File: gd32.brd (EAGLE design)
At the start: 55 x 70 mm, 23 parts, among them IC1 GD32F450IKH6, IC2 AMS1117-1.5, J1 LCD, U1 W9825G6KH-5

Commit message: Incremental changes
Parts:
- removed POWER1: DC-005, sjg-power:DCJ3P-14.2X11.0X9.0MM
- added +5V_IN: DC-005, sjg-power:DCJ3P-14.2X11.0X9.0MM
- added BOOT_SEL: B3F-1005, SparkFun:TACTILE-PTH
- added BOOT_WHICH: JS202011SCQN, samacsys:JS202011SCQN
- added C10, C9: 10uF/16v, rcl:C0603
- added C11: 0.1uF, rcl:C0201
- added D1: GRN-0402, Seeed-LED:LED-0402
- added JP2: (no value), pinhead:1X02
- added R4: 470R, rcl:R0402
- added R5: 10K, rcl:R0402
- added U$1: GD32_DEBUG, sjg-stm32:SWD_DEBUG
- IC2: value AMS1117-1.5 -> AMS1117-3.3
- moved IC2 40.0 mm to (41.0, 75.5), turned to 0 degrees
- moved POWER 32.4 mm to (26.2, 73.5), turned to 90 degrees
- moved H4 14.1 mm to (61.0, 76.0)
- moved H1 10.0 mm to (4.00, 76.0)
- moved H3 10.0 mm to (61.0, 4.00)
- moved J1 4.00 mm to (28.8, 4.37)
- moved JP1 3.00 mm to (12.0, 4.37)
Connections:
- new net BOOT0: BOOT_SEL.3, BOOT_SEL.4, IC1.D6, R5.2
- new net N$2: D1.+, R4.2
- new net N$3: C10.1, IC2.2, IC2.4, JP2.2, R4.1
- net +3V3: now also BOOT_SEL.1, BOOT_SEL.2, BOOT_WHICH.1, BOOT_WHICH.6, JP2.1, U$1.P1; no longer IC2.2, IC2.4
- net +5V: now also C9.1
- net GND: now also +5V_IN.-1, +5V_IN.-2, BOOT_WHICH.3, BOOT_WHICH.4, C10.2, C11.2, C9.2, R5.1, U$1.P3, U$1.P5, U$1.P9; no longer POWER1.-1, POWER1.-2
- net PA13: now also U$1.P2
- net PA14: now also U$1.P4
- net PB10: now also U$1.P6
- net PB11: now also U$1.P8
- net PB2: now also BOOT_WHICH.2, BOOT_WHICH.5
- net PB4: now also C11.1, U$1.P10
- net V+: now also +5V_IN.+; no longer POWER1.+
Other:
- board size 55 x 70 mm -> 65 x 80 mm
- board text added: "BL"
- board text added: "SRAM"

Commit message: Ready for manufacture
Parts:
- removed C11: 0.1uF, rcl:C0201
- removed JP1: (no value), pinhead:2X02
- removed JP2: (no value), pinhead:1X02
- removed U$1: GD32_DEBUG, sjg-stm32:SWD_DEBUG
- added BL_CTRL, I2C1, SPI0, SPI1, SPI2: (no value), pinhead:2X02
- added C12, C13: 15pF, rcl:C0201
- added C14, C15, C16, C17, C18, C19, C20, C21, C22, C23, C24, C25, C26, C27, C28, C34: 0.1uF, rcl:C0201
- added IO_EXT: (no value), pinhead:2X20
- added PASS_3V3, PASS_RST: (no value), pinhead:1X02
- added PROG: GD32_DEBUG, sjg-stm32:SWD_DEBUG
- added Q2: 8MHz, adafruit:NX3225
- added R37, R8: 1K5, rcl:R0603
- added R6, R7: 10K, rcl:R0402
- added RESET: B3F-1005, SparkFun:TACTILE-PTH
- R2, R3: device rcl:R0805 -> rcl:R0402
- moved R5 10.2 mm to (54.0, 16.6)
- moved R3 7.55 mm to (20.2, 32.1)
- moved R2 7.24 mm to (20.2, 30.9)
- moved IC1 7.09 mm to (29.2, 25.4)
- moved C7 6.50 mm to (38.0, 60.0)
- moved C6 6.46 mm to (38.0, 55.3)
- moved C1 6.14 mm to (20.8, 62.4)
- moved C2 6.11 mm to (20.8, 57.7)
- moved U1 6.08 mm to (29.2, 53.6)
- moved C3 6.08 mm to (20.8, 64.0)
- moved C4 6.08 mm to (20.8, 53.6)
- moved C5 6.08 mm to (20.8, 43.2)
- moved C8 3.24 mm to (3.87, 23.6)
- moved R1 3.24 mm to (5.87, 23.6)
- moved +5V_IN 2.54 mm to (17.0, 69.2)
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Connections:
- net PA11 renamed MCU_USB_N
- net PA12 renamed MCU_USB_P
- removed net PB4: C11.1, IC1.A9, U$1.P10
- removed net PD13: IC1.M15
- removed net PE2: IC1.A2
- removed net PE3: IC1.A1
- removed net PG13: IC1.A8
- removed net PG14: IC1.A7, U1.17
- removed net PG3: IC1.K15
- removed net PG9: IC1.C10
- removed net PH6: IC1.M11
- removed net PH7: IC1.N12
- removed net PI11: IC1.E4
- new net !RST!: IC1.J1, PASS_RST.2, R7.1, RESET.3, RESET.4
- new net N$4: IC1.C6, R6.1
- new net N$5: PASS_RST.1, PROG.P10
- net +3V3: now also BL_CTRL.1, C14.1, C15.1, C16.1, C17.1, C18.1, C19.1, C20.1, C21.1, C22.1, C23.1, C24.1, C25.1, C26.1, C27.1, C28.1, C34.1, I2C1.1, IC1.C1, IC1.C5, IC1.C7, IC1.C8, IC1.C9, IC1.F3, IC1.G13, IC1.G3, IC1.H13, IC1.J12, IC1.J13, IC1.K4, IC1.N10, IC1.N8, IC1.N9, IC1.P1, IC1.R1, IO_EXT.2, PASS_3V3.1, PROG.P1, R37.2, R6.2, R7.2, R8.2; no longer JP1.1, JP2.1, U$1.P1
- net +5V: now also IO_EXT.1
- net GND: now also C12.2, C13.2, C14.2, C15.2, C16.2, C17.2, C18.2, C19.2, C20.2, C21.2, C22.2, C23.2, C24.2, C25.2, C26.2, C27.2, C28.2, C34.2, D1.-, I2C1.3, IC1.D5, IC1.D7, IC1.D8, IC1.D9, IC1.F10, IC1.F12, IC1.F2, IC1.F6, IC1.F7, IC1.F8, IC1.F9, IC1.G10, IC1.G12, IC1.G2, IC1.G6, IC1.G7, IC1.G8, IC1.G9, IC1.H10, IC1.H12, IC1.H6, IC1.H7, IC1.H8, IC1.H9, IC1.J10, IC1.J6, IC1.J7, IC1.J8, IC1.J9, IC1.K10, IC1.K6, IC1.K7, IC1.K8, IC1.K9, IC1.M1, IC1.M8, IC1.M9, IC1.N1, IO_EXT.19, IO_EXT.20, IO_EXT.39, IO_EXT.40, PROG.P3, PROG.P5, PROG.P9, Q2.2, Q2.4, RESET.1, RESET.2, SPI0.3, SPI1.3, SPI2.3; no longer C11.2, U$1.P3, U$1.P5, U$1.P9
- net LCD_BL: now also BL_CTRL.2, BL_CTRL.4; no longer JP1.2, JP1.4
- net N$3: now also PASS_3V3.2; no longer JP2.2
- net PA0: now also IO_EXT.37
- net PA1: now also IO_EXT.38
- net PA13: now also PROG.P2; no longer U$1.P2
- net PA14: now also PROG.P4; no longer U$1.P4
- net PA15: now also IO_EXT.31
- net PA2: now also IO_EXT.35
- net PA3: now also IO_EXT.36
- net PA4: now also BL_CTRL.3; no longer JP1.3
- net PA5: now also SPI0.2
- net PA6: now also SPI0.4
- net PA7: now also SPI0.1
- net PA8: now also IO_EXT.33
- net PA9: now also IO_EXT.34
- net PB0: now also IO_EXT.32
- net PB1: now also IO_EXT.29
- net PB10: now also PROG.P6; no longer U$1.P6
- net PB11: now also PROG.P8; no longer U$1.P8
- net PB12: now also IO_EXT.26
- net PB13: now also SPI1.2
- net PB14: now also SPI1.4
- net PB15: now also SPI1.1
- net PB3: now also IO_EXT.30
- net PB7: now also IO_EXT.27
- net PB8: now also IO_EXT.28
- net PB9: now also IO_EXT.25
- net PC0: now also IO_EXT.23
- net PC1: now also IO_EXT.24
- net PC10: now also SPI2.2
- net PC11: now also SPI2.4
- net PC12: now also SPI2.1
- net PC13: now also IO_EXT.11
- net PC14: now also IO_EXT.12
- net PC15: now also IO_EXT.9
- net PC2: now also IO_EXT.21
- net PC3: now also IO_EXT.22
- net PC4: now also IO_EXT.17
- net PC5: now also IO_EXT.18
- net PC6: now also IO_EXT.15
- net PC7: now also IO_EXT.16
- net PC8: now also IO_EXT.13
- net PC9: now also IO_EXT.14
- net PD11: now also IO_EXT.3
- net PD12: now also IO_EXT.4
- net PD2: now also IO_EXT.10
- net PD3: now also IO_EXT.7
- net PD4: now also IO_EXT.8
- net PD6: now also IO_EXT.5
- net PD7: now also IO_EXT.6
- net PG15: now also U1.17
- net PH0: now also C12.1, Q2.1; no longer J1.40
- net PH1: now also C13.1, Q2.3; no longer J1.39
- net PH4: now also I2C1.2, R8.1
- net PH5: now also I2C1.4, R37.1
- net PI3: now also J1.40
- net PI8: now also J1.39
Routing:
- net PA5: track 0.00 -> 180.4 mm, vias 0 -> 2
- net +5V: track 0.00 -> 161.0 mm
- net PI3: track 0.00 -> 160.3 mm, vias 0 -> 8
- net PB10: track 0.00 -> 148.8 mm, vias 0 -> 4
- net PB11: track 0.00 -> 127.7 mm, vias 0 -> 4
- net PD7: track 0.00 -> 121.6 mm, vias 0 -> 3
- net PA4: track 0.00 -> 117.4 mm, vias 0 -> 6
- net PB8: track 0.00 -> 114.8 mm, vias 0 -> 5
- net PD3: track 0.00 -> 112.4 mm, vias 0 -> 6
- net GND: track 0.00 -> 108.5 mm, vias 0 -> 84
- net PB3: track 0.00 -> 105.1 mm, vias 0 -> 4
- net PD2: track 0.00 -> 103.1 mm, vias 0 -> 5
- net PF1: track 0.00 -> 101.4 mm, vias 0 -> 6
- net PD4: track 0.00 -> 100.1 mm, vias 0 -> 5
- net PC13: track 0.00 -> 98.1 mm, vias 0 -> 5
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- added copper zone on layer 15, net +3V3
- added copper zone on layer 2, net GND
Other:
- board text added: ""Atomic" RGB i/o"
- board text added: "+3V3"
- board text added: "+3v3"
- board text added: "+5V"
- board text added: "1"
- board text added: "40"
- board text added: "CK"
- board text added: "GD32-LCD v 0.1 © 2022 SjG"
- board text added: "GND"
- board text added: "ON"
- board text added: "PA0"
- board text added: "PA1"
- board text added: "PA15"
- board text added: "PA2"
- board text added: "PA3"
- board text added: "PA4"
- board text added: "PA8"
- board text added: "PA9"
- board text added: "PB0"
- board text added: "PB1"
- board text added: "PB12"
- board text added: "PB3"
- board text added: "PB7"
- board text added: "PB8"
- board text added: "PB9"
- board text added: "PC0"
- board text added: "PC1"
- board text added: "PC13"
- board text added: "PC14"
- board text added: "PC15"
- board text added: "PC2"
- board text added: "PC3"
- board text added: "PC4"
- board text added: "PC5"
- board text added: "PC6"
- board text added: "PC7"
- board text added: "PC8"
- board text added: "PC9"
- board text added: "PD11"
- board text added: "PD12"
- board text added: "PD2"
- board text added: "PD3"
- board text added: "PD4"
- board text added: "PD6"
- board text added: "PD7"
- board text added: "RX"
- board text added: "SCL"
- board text added: "SDA"
- board text added: "TX"

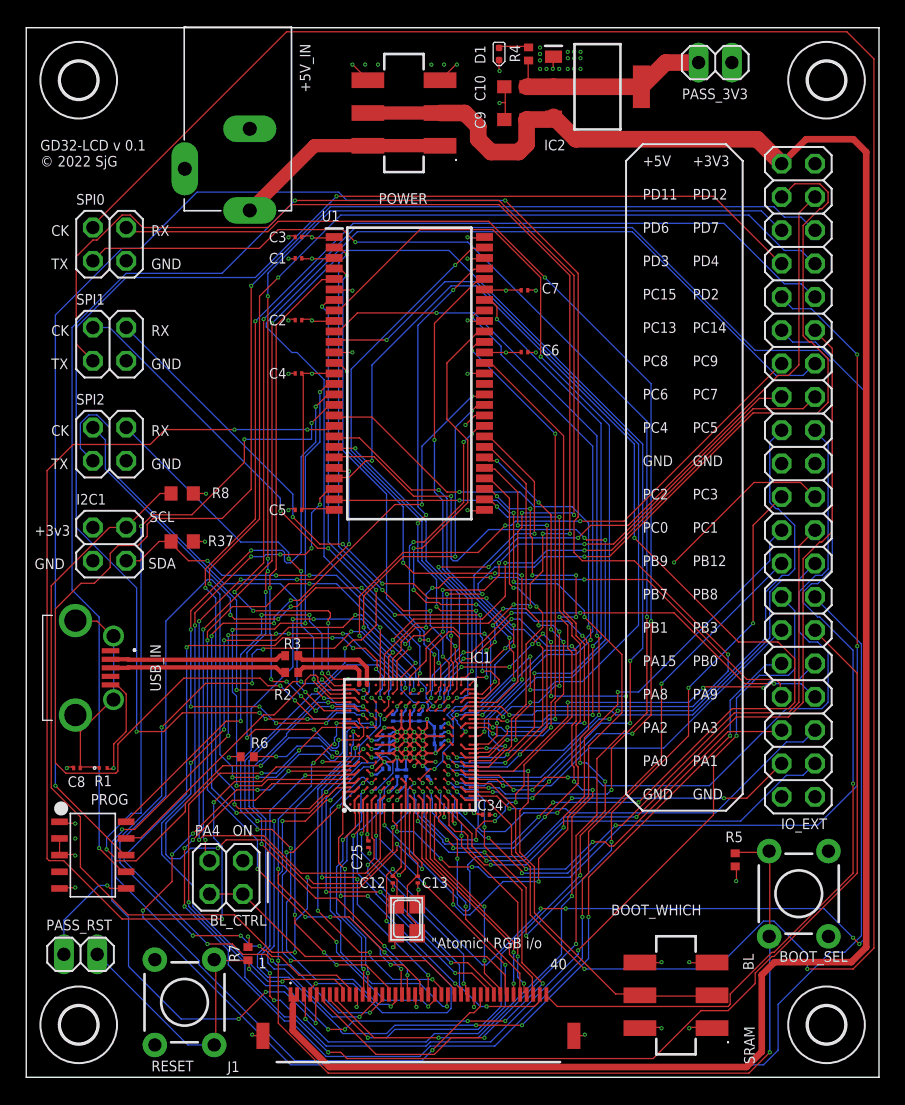
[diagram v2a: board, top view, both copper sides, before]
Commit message: Sent off for manufacture, with corrected 1K5 pullups on I2C
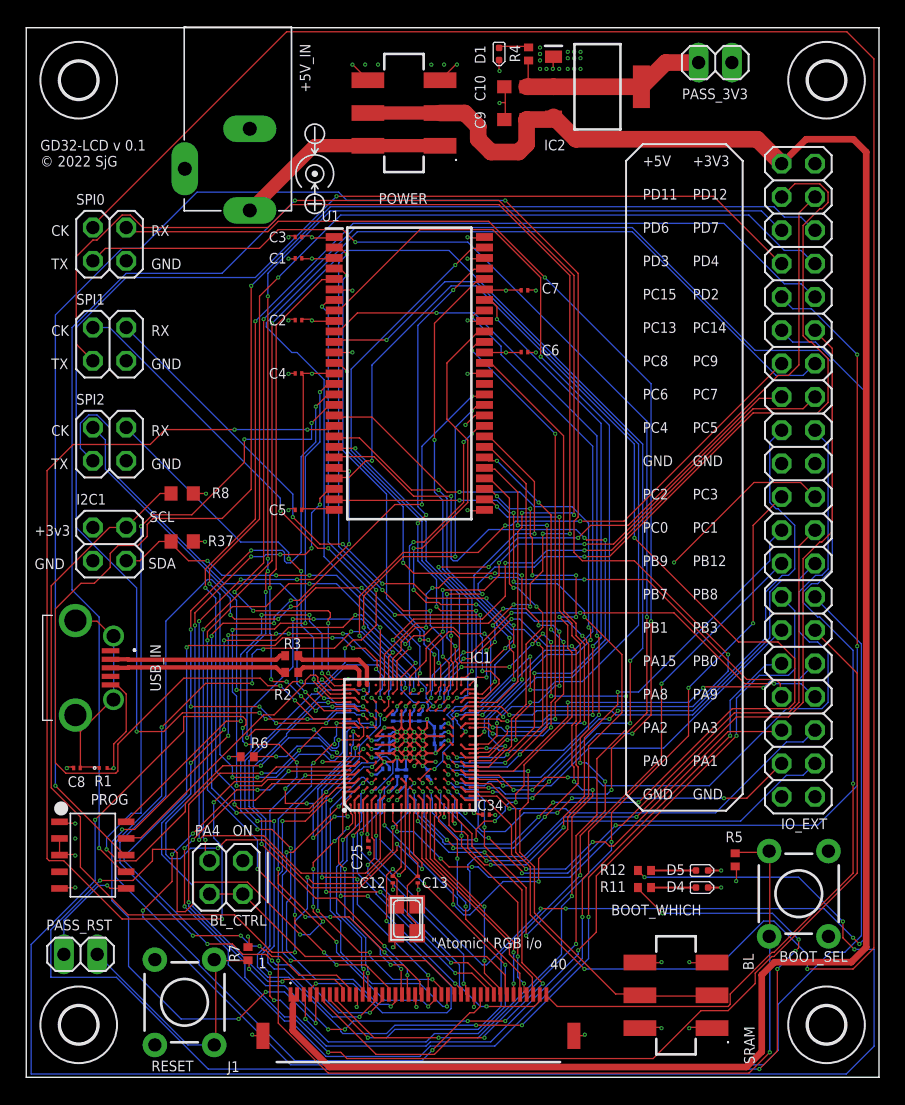
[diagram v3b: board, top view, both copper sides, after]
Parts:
- added D4, D5: GRN-0402, Seeed-LED:LED-0402
- added R11, R12: 470R, rcl:R0402
- IC1: value GD32F450IKH6 -> GD32F450
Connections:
- new net LED0: IC1.A2, R12.1
- new net LED1: IC1.A1, R11.1
- new net N$8: D4.+, R11.2
- new net N$9: D5.+, R12.2
- net GND: now also D4.-, D5.-
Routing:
- net LED0: track 0.00 -> 150.5 mm, vias 0 -> 12
- net LED1: track 0.00 -> 128.5 mm, vias 0 -> 12
- net N$9: track 0.00 -> 3.42 mm
- net N$8: track 0.00 -> 3.42 mm
- net GND: track 108.5 -> 110.5 mm, vias 84 -> 86

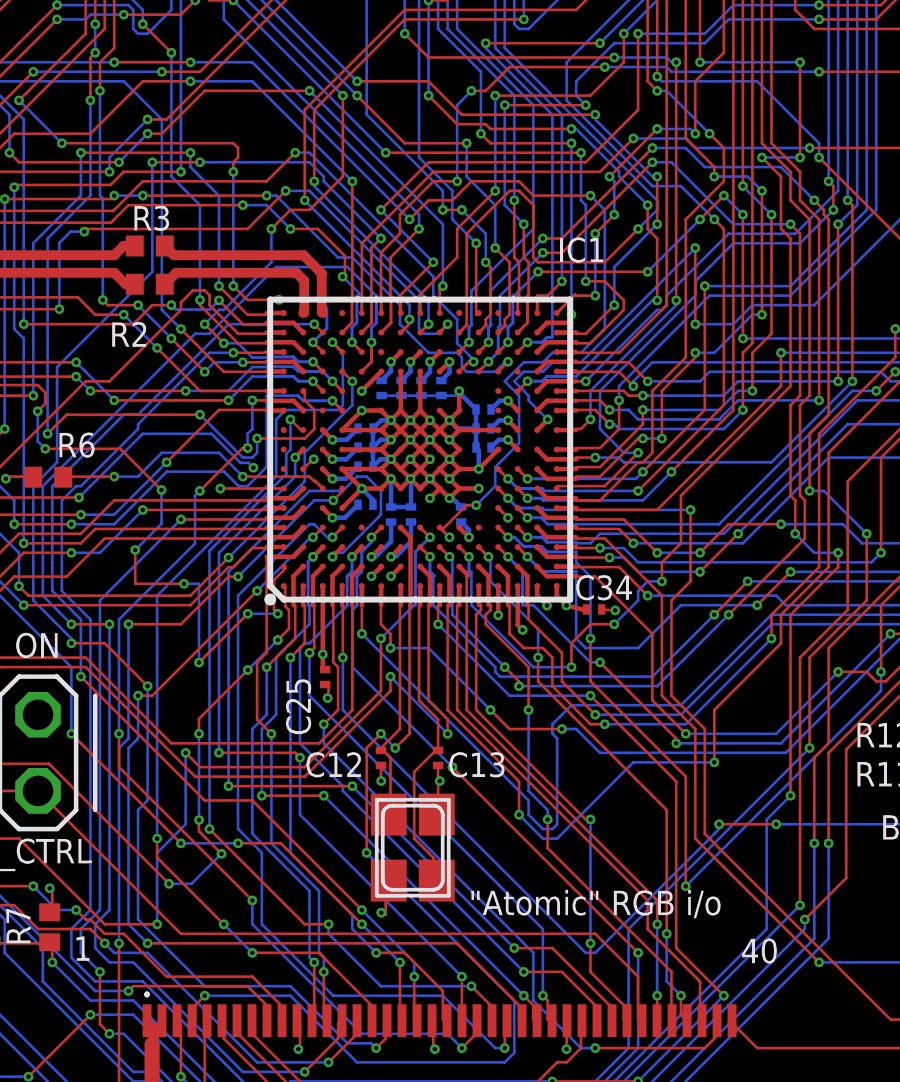
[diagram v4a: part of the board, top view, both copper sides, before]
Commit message: Alter the pad sizes in the GD32 library
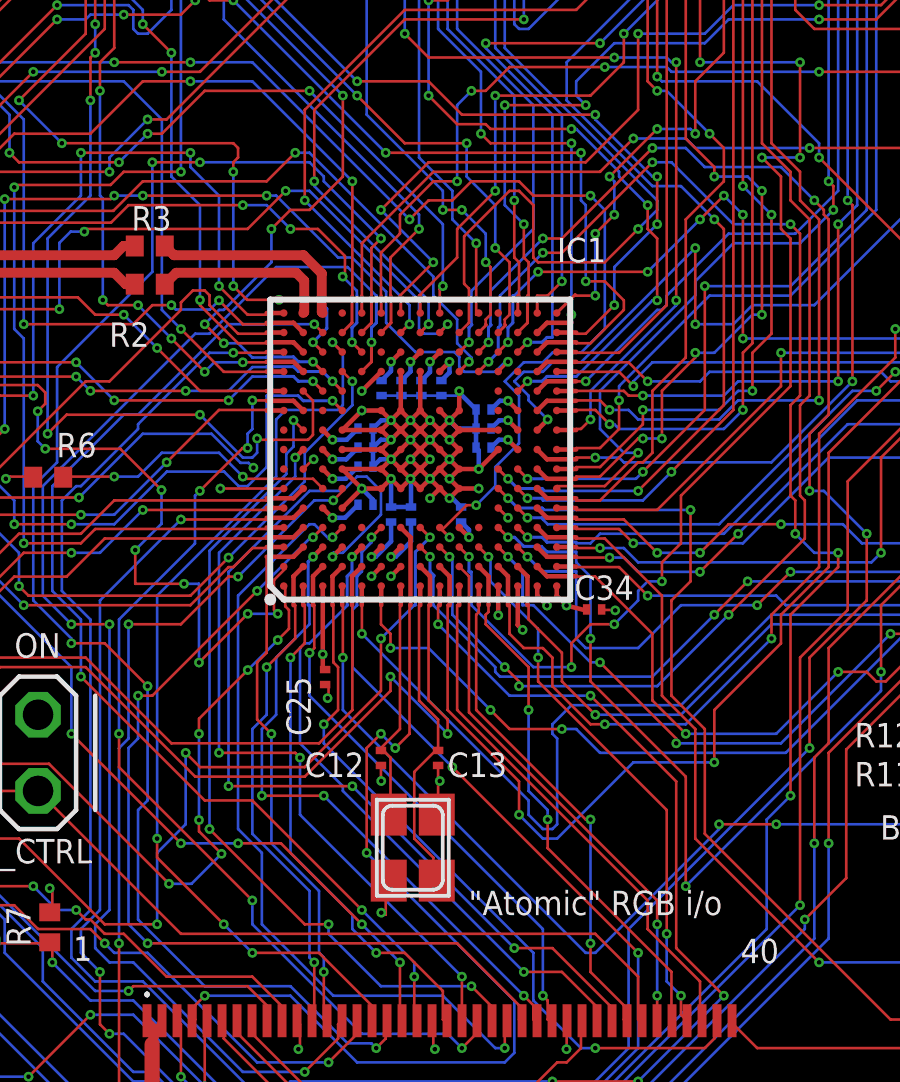
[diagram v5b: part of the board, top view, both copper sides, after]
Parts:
- IC1: device samacsys:BGA201C65P15X15_1000X1000X84 -> gd32:BGA201C65P15X15_1000X1000X84
